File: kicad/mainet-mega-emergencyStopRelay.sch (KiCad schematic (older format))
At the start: 41 parts, among them J102 Screw_Terminal_01x02, J38 Screw_Terminal_01x01, J39 Screw_Terminal_01x01, J41 Screw_Terminal_01x01, J43 Screw_Terminal_01x01, J45 Screw_Terminal_01x01, J46 Screw_Terminal_01x01, J47 Screw_Terminal_01x01, J48 Screw_Terminal_01x01, J49 Screw_Terminal_01x01, J50 Screw_Terminal_01x01, J51 Screw_Terminal_01x01, J52 Screw_Terminal_01x01, J53 Screw_Terminal_01x01, J54 Screw_Terminal_01x01, J55 Screw_Terminal_01x01, J56 Screw_Terminal_01x01, J57 Screw_Terminal_01x01, J58 Screw_Terminal_01x01, J59 Screw_Terminal_01x01, J60 Screw_Terminal_01x01, J61 Screw_Terminal_01x01, J62 Screw_Terminal_01x01, J63 Screw_Terminal_01x01, K10 Contactor-3-poles, K11 relay-4p2t, K9 relay-4p2t, SW5 emergencyStop, T1 Transformer_2P_1S, U11 socket-4p2t, U17 socket-4p2t

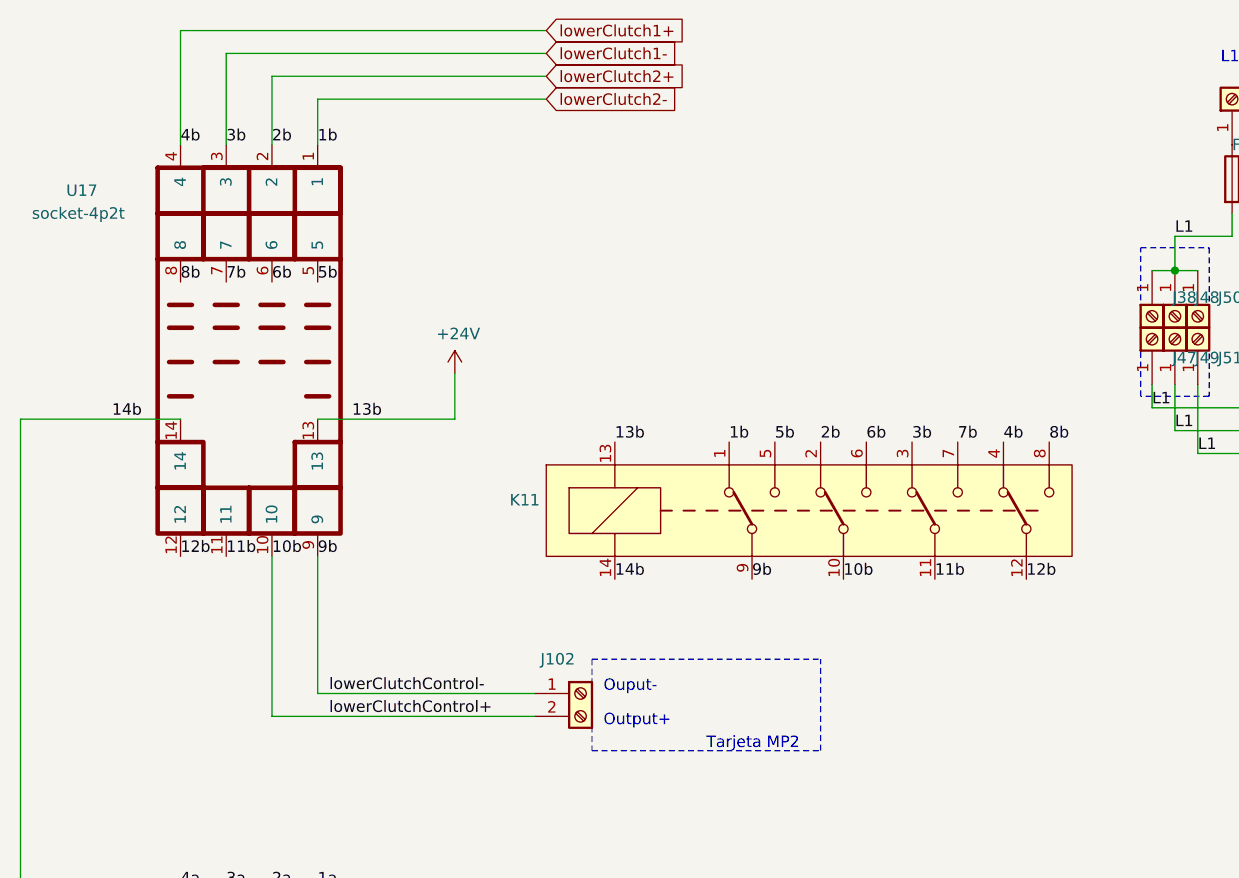
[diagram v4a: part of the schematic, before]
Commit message: KICAD: Reorganizar .sch relé de parada
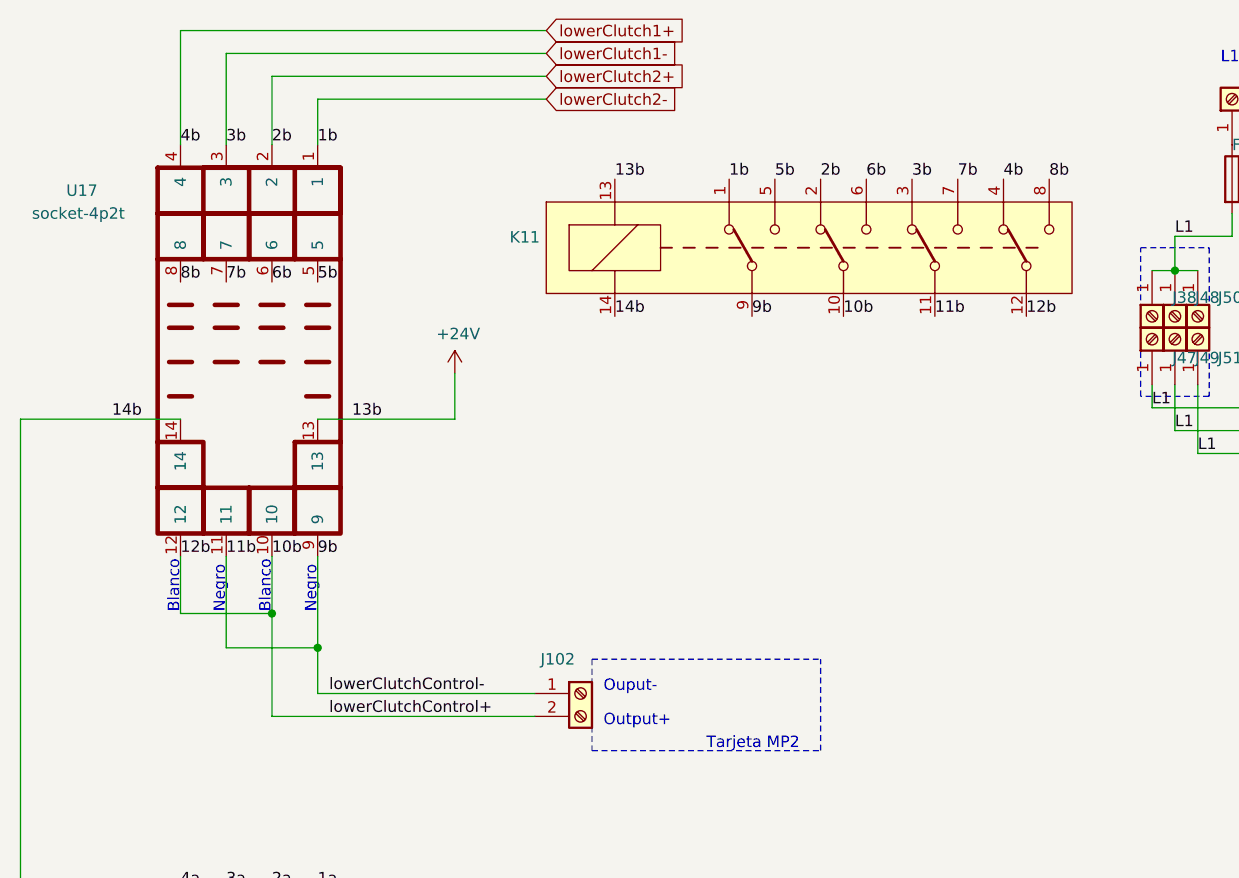
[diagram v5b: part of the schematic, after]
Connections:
- net 12b is gone; now on net 10b: K11.12 (C4), U17.12
- net 9b is gone; now on net 11b: J102.1 (Pin_1), K11.9 (C1), U17.9
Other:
- note added: "Blanco"
- note added: "Negro"
- moved on the sheet: K11
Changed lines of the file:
@@
 L mainet-mega-rescue:relay-4p2t-ng-relays K?
 U 1 1 611801A8
-P 4200 2750
+P 4200 1600
 AR Path="/611801A8" Ref="K?"  Part="1"
 AR Path="/5FF9030A/611801A8" Ref="K11"  Part="1"
-F 0 "K11" H 2972 2796 50  0000 R CNN
-F 1 "relay-4p2t" H 2972 2705 50  0001 R CNN
-F 2 "" H 4650 3650 50  0001 C CNN
-F 3 "" H 4650 3650 50  0001 C CNN
-	1    4200 2750
-	1    0    0    -1
-$EndComp
-Text Label 5200 2450 0    50   ~ 0
+F 0 "K11" H 2972 1646 50  0000 R CNN
+F 1 "relay-4p2t" H 2972 1555 50  0001 R CNN
+F 2 "" H 4650 2500 50  0001 C CNN
+F 3 "" H 4650 2500 50  0001 C CNN
+	1    4200 1600
+	1    0    0    -1
+$EndComp
+Text Label 5200 1300 0    50   ~ 0
 8b
-Text Label 4000 2450 0    50   ~ 0
+Text Label 4000 1300 0    50   ~ 0
 5b
-Text Label 4400 2450 0    50   ~ 0
+Text Label 4400 1300 0    50   ~ 0
 6b
-Text Label 4800 2450 0    50   ~ 0
+Text Label 4800 1300 0    50   ~ 0
 7b
-Text Label 4200 2450 0    50   ~ 0
+Text Label 4200 1300 0    50   ~ 0
 2b
-Text Label 4600 2450 0    50   ~ 0
+Text Label 4600 1300 0    50   ~ 0
 3b
-Text Label 5000 2450 0    50   ~ 0
+Text Label 5000 1300 0    50   ~ 0
 4b
-Text Label 4300 3050 0    50   ~ 0
+Text Label 4300 1900 0    50   ~ 0
 10b
-Text Label 3900 3050 0    50   ~ 0
+Text Label 3900 1900 0    50   ~ 0
 9b
-Text Label 5100 3050 0    50   ~ 0
+Text Label 5100 1900 0    50   ~ 0
 12b
-Text Label 3800 2450 0    50   ~ 0
+Text Label 3800 1300 0    50   ~ 0
 1b
-Text Label 3300 2450 0    50   ~ 0
+Text Label 3300 1300 0    50   ~ 0
 13b
-Text Label 3300 3050 0    50   ~ 0
+Text Label 3300 1900 0    50   ~ 0
 14b
 Wire Wire Line
@@
 Wire Wire Line
 	3050 5450 3050 5600
-Text Label 4700 3050 0    50   ~ 0
+Text Label 4700 1900 0    50   ~ 0
 11b
 Text Label 2150 2350 0    50   ~ 0
@@
 	4200 3800 4200 3400
 Wire Wire Line
-	1800 2950 1800 3650
-Wire Wire Line
-	2000 2950 2000 3550
+	1800 2950 1800 3200
 Text Label 2050 3550 0    50   ~ 0
 lowerClutchControl-
@@
 Wire Wire Line
 	2000 950  2000 1150
+Wire Wire Line
+	1800 3200 1400 3200
+Wire Wire Line
+	1400 3200 1400 2950
+Connection ~ 1800 3200
+Wire Wire Line
+	1800 3200 1800 3650
+Text Notes 1800 3200 1    50   ~ 0
+Blanco
+Text Notes 1400 3200 1    50   ~ 0
+Blanco
+Text Notes 2000 3200 1    50   ~ 0
+Negro
+Wire Wire Line
+	2000 2950 2000 3350
+Wire Wire Line
+	1600 3350 2000 3350
+Connection ~ 2000 3350
+Wire Wire Line
+	2000 3350 2000 3550
+Wire Wire Line
+	1600 2950 1600 3350
+Text Notes 1600 3200 1    50   ~ 0
+Negro
 $EndSCHEMATC
